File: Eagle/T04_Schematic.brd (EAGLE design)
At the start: 40.6 x 63.5 mm, 29 parts, among them Y1 16 MHz

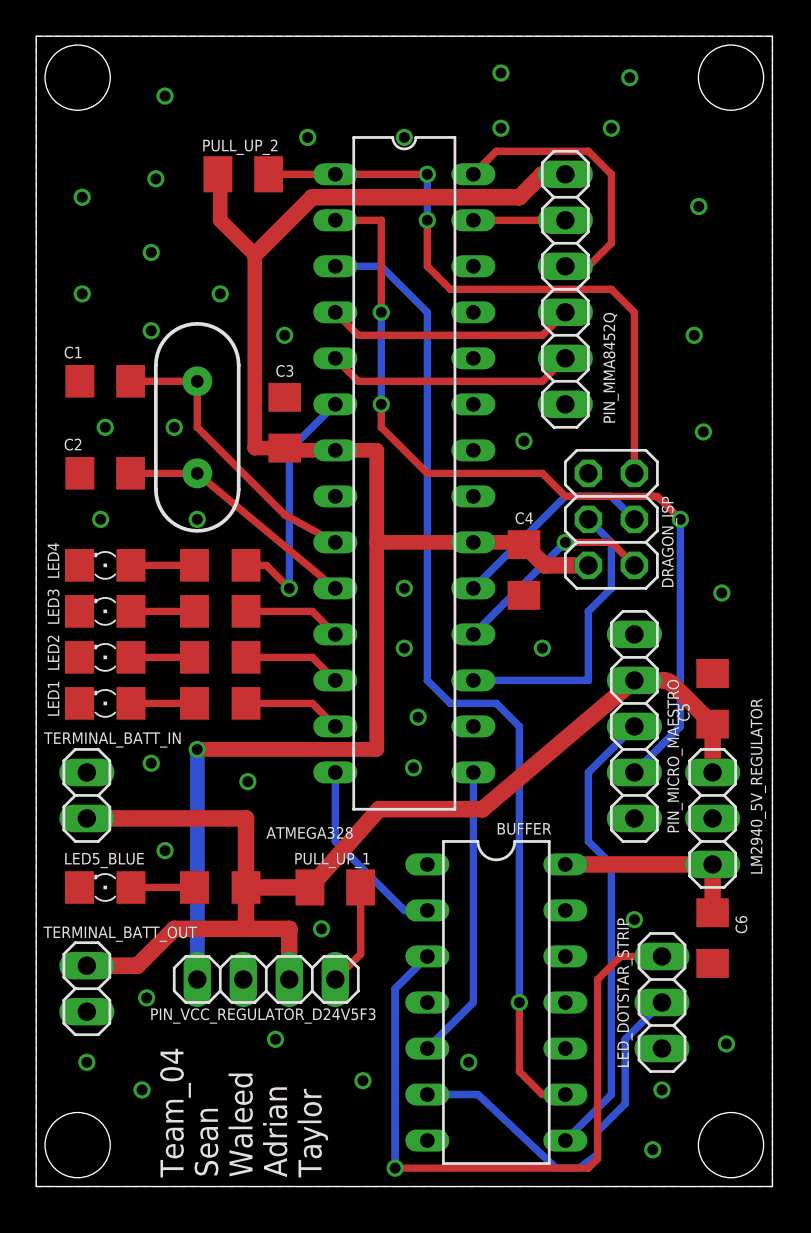
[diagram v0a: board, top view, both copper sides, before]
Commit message: Final(?) Layout
Increase board size for more room to solder.
Improved power signal layout.
Added missing GND and VCC to Dotstar LEDs.
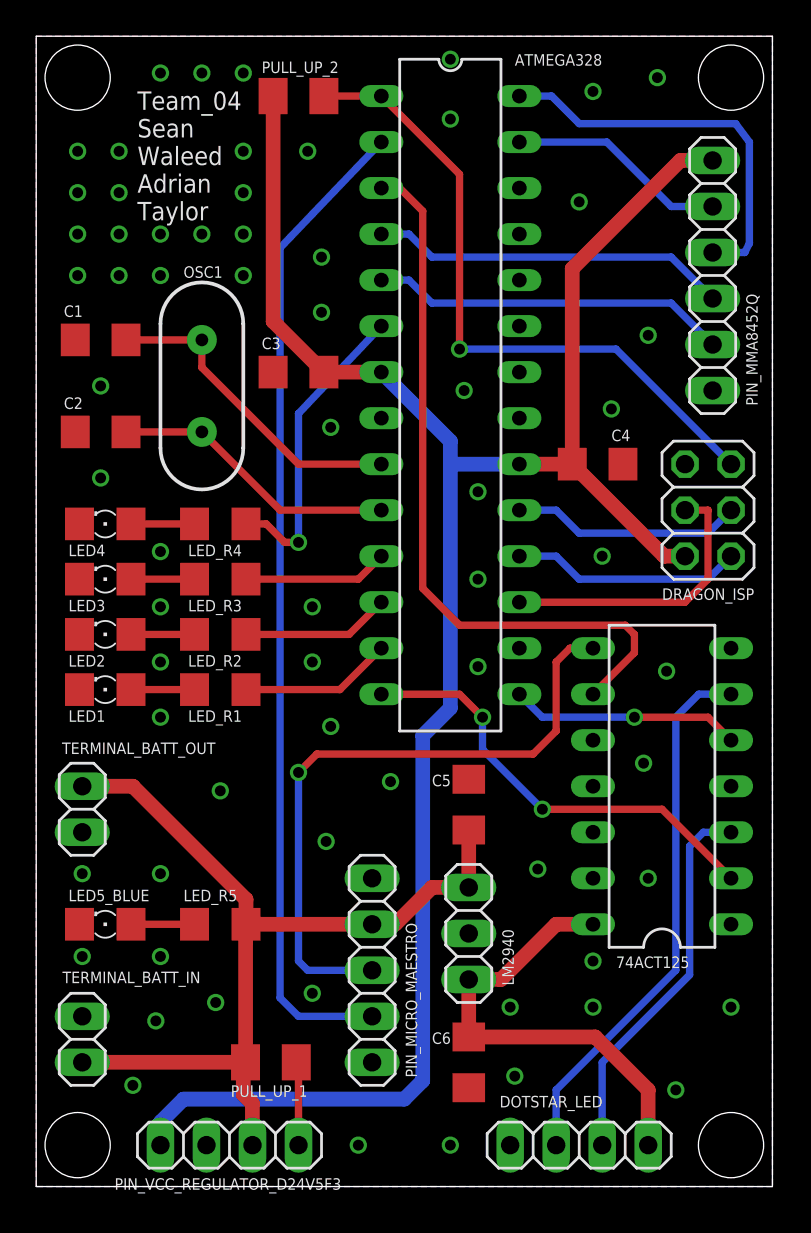
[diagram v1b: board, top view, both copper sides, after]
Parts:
- removed BUFFER: 74ACT125N, 74xx-eu:DIL14
- removed LED_DOTSTAR_STRIP: 1x3, pinhead:1X03
- removed LED_RESISTOR_1, LED_RESISTOR_2, LED_RESISTOR_3, LED_RESISTOR_4, LED_RESISTOR_5: TBD Resistance, rcl:R1206
- removed LM2940_5V_REGULATOR: (no value), pinhead:1X03
- removed Y1: 16 MHz, SparkFun-FreqCtrl:HC49US
- added 74ACT125: 74ACT125N, 74xx-eu:DIL14
- added DOTSTAR_LED: 1x4, pinhead:1X04
- added LED_R1, LED_R2, LED_R3, LED_R4, LED_R5: TBD Resistance, rcl:R1206
- added LM2940: 1x3, pinhead:1X03
- added OSC1: 16 MHz, SparkFun-FreqCtrl:HC49US
- moved PIN_MICRO_MAESTRO 19.8 mm to (18.5, 11.9)
- moved C6 15.1 mm to (23.9, 6.86)
- moved C5 14.7 mm to (23.9, 21.1)
- moved TERMINAL_BATT_IN 13.5 mm to (2.54, 8.13)
- moved PULL_UP_1 10.3 mm to (13.0, 6.86)
- moved TERMINAL_BATT_OUT 9.91 mm to (2.54, 20.8)
- moved PIN_VCC_REGULATOR_D24V5F3 9.37 mm to (10.7, 2.29)
- moved PIN_MMA8452Q 8.16 mm to (37.3, 50.3)
- moved C4 7.12 mm to (31.0, 39.9), turned to 0 degrees
- moved DRAGON_ISP 5.36 mm to (37.1, 37.3)
- moved PULL_UP_2 5.29 mm to (14.5, 60.2)
- moved ATMEGA328 5.01 mm to (22.9, 43.7)
- moved C3 2.90 mm to (14.5, 45.0), turned to 180 degrees
- moved C2 2.30 mm to (3.56, 41.7)
- moved C1 2.30 mm to (3.56, 46.7)
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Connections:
- net 5V_VCC: now also 74ACT125.14, DOTSTAR_LED.1, LM2940.3; no longer BUFFER.14, LM2940_5V_REGULATOR.3
- net CLOCK: now also 74ACT125.2; no longer BUFFER.2
- net DATA: now also 74ACT125.5; no longer BUFFER.5
- net GND: now also 74ACT125.1, 74ACT125.10, 74ACT125.4, 74ACT125.7, DOTSTAR_LED.4, LM2940.2; no longer BUFFER.1, BUFFER.10, BUFFER.4, BUFFER.7, LED_DOTSTAR_STRIP.3, LM2940_5V_REGULATOR.2
- net N$1: now also LED_R5.2; no longer LED_RESISTOR_5.2
- net N$10: now also LED_R2.1; no longer LED_RESISTOR_2.1
- net N$11: now also LED_R4.1; no longer LED_RESISTOR_4.1
- net N$12: now also LED_R1.1; no longer LED_RESISTOR_1.1
- net N$13: now also 74ACT125.6, DOTSTAR_LED.3; no longer BUFFER.6, LED_DOTSTAR_STRIP.2
- net N$2: now also LED_R1.2; no longer LED_RESISTOR_1.2
- net N$3: now also LED_R2.2; no longer LED_RESISTOR_2.2
- net N$4: now also LED_R3.2; no longer LED_RESISTOR_3.2
- net N$5: now also LED_R4.2; no longer LED_RESISTOR_4.2
- net N$8: now also 74ACT125.3, DOTSTAR_LED.2; no longer BUFFER.3, LED_DOTSTAR_STRIP.1
- net N$9: now also LED_R3.1; no longer LED_RESISTOR_3.1
- net RXD: now also 74ACT125.8; no longer BUFFER.8
- net UP_TXD: now also 74ACT125.9; no longer BUFFER.9
- net VCC_6V: now also LED_R5.1, LM2940.1; no longer LED_RESISTOR_5.1, LM2940_5V_REGULATOR.1
- net XTAL1: now also OSC1.1; no longer Y1.1
- net XTAL2: now also OSC1.2; no longer Y1.2
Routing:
- net VCC: track 93.1 -> 113.7 mm, vias 1 -> 0
- net N$8: track 37.8 -> 21.1 mm, vias 1 -> 0
- net 5V_VCC: track 10.8 -> 25.5 mm
- net CLOCK: track 10.5 -> 24.6 mm, vias 0 -> 2
- net UP_TXD: track 54.7 -> 40.6 mm, vias 1 -> 0
- net VCC_6V: track 63.6 -> 50.8 mm
- net RXD: track 25.5 -> 36.0 mm, vias 0 -> 1
- net N$13: track 21.1 -> 29.9 mm
- net SERVO_TXD: track 47.8 -> 55.0 mm, vias 3 -> 0
- net SDA: track 5.08 -> 12.1 mm
- net SCL: track 15.5 -> 21.8 mm
- net INT0: track 13.8 -> 19.8 mm
- net INT1: track 13.8 -> 19.8 mm
- net DATA: track 16.3 -> 12.7 mm, vias 0 -> 1
- net N$12: track 5.45 -> 8.41 mm
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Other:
- board text removed: "Expand to fit space: 1.6'' x 2.5'' Make it easier to solder"

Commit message: Fixed Typo in Component Name
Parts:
- renumbered PIN_VCC_REGULATOR_D24V5F3 to D24V5F3
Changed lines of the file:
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@@
 <attribute name="NAME" x="39.8272" y="43.1038" size="0.635" layer="25" ratio="10" rot="R90"/>
 </element>
-<element name="PIN_VCC_REGULATOR_D24V5F3" library="pinhead" package="1X04" value="1x4" x="10.668" y="2.286" smashed="yes" rot="R180">
-<attribute name="NAME" x="16.8402" y="0.4572" size="0.635" layer="25" ratio="10" rot="R180"/>
+<element name="D24V5F3" library="pinhead" package="1X04" value="1x4" x="10.668" y="2.286" smashed="yes" rot="R180">
+<attribute name="NAME" x="6.2738" y="4.1148" size="0.635" layer="25" ratio="10"/>
 </element>
 <element name="PULL_UP_1" library="rcl" package="M1206" value="10K" x="12.954" y="6.858" smashed="yes" rot="R180">
@@
 <contactref element="LED3" pad="C"/>
 <contactref element="LED4" pad="C"/>
-<contactref element="PIN_VCC_REGULATOR_D24V5F3" pad="3"/>
+<contactref element="D24V5F3" pad="3"/>
 <contactref element="TERMINAL_BATT_OUT" pad="2"/>
 <contactref element="PIN_MICRO_MAESTRO" pad="1"/>
@@
 </signal>
 <signal name="VCC">
-<contactref element="PIN_VCC_REGULATOR_D24V5F3" pad="4"/>
+<contactref element="D24V5F3" pad="4"/>
 <contactref element="PULL_UP_2" pad="2"/>
 <contactref element="ATMEGA328" pad="20"/>
@@
 </signal>
 <signal name="V_REG_RESET">
-<contactref element="PIN_VCC_REGULATOR_D24V5F3" pad="1"/>
+<contactref element="D24V5F3" pad="1"/>
 <contactref element="PULL_UP_1" pad="1"/>
 <wire x1="14.354" y1="6.858" x2="14.478" y2="6.734" width="0.4064" layer="1"/>
@@
 <contactref element="TERMINAL_BATT_IN" pad="2"/>
 <contactref element="TERMINAL_BATT_OUT" pad="1"/>
-<contactref element="PIN_VCC_REGULATOR_D24V5F3" pad="2"/>
+<contactref element="D24V5F3" pad="2"/>
 <contactref element="PULL_UP_1" pad="2"/>
 <contactref element="PIN_MICRO_MAESTRO" pad="2"/>

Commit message: Minor Tweaks and Fixes
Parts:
- moved C4 0.25 mm to (31.2, 39.9)
- renumbered PIN_MICRO_MAESTRO to MICRO_MAESTRO, PIN_MMA8452Q to MMA8452Q
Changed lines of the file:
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@@
 <layer number="17" name="Pads" color="2" fill="1" visible="yes" active="yes"/>
 <layer number="18" name="Vias" color="2" fill="1" visible="yes" active="yes"/>
-<layer number="19" name="Unrouted" color="6" fill="1" visible="yes" active="yes"/>
+<layer number="19" name="Unrouted" color="6" fill="1" visible="no" active="yes"/>
 <layer number="20" name="Dimension" color="15" fill="1" visible="yes" active="yes"/>
 <layer number="21" name="tPlace" color="7" fill="1" visible="yes" active="yes"/>
@@
 <layer number="45" name="Holes" color="7" fill="1" visible="yes" active="yes"/>
 <layer number="46" name="Milling" color="3" fill="1" visible="no" active="yes"/>
-<layer number="47" name="Measures" color="7" fill="1" visible="yes" active="yes"/>
-<layer number="48" name="Document" color="7" fill="1" visible="yes" active="yes"/>
-<layer number="49" name="Reference" color="7" fill="1" visible="yes" active="yes"/>
+<layer number="47" name="Measures" color="7" fill="1" visible="no" active="yes"/>
+<layer number="48" name="Document" color="7" fill="1" visible="no" active="yes"/>
+<layer number="49" name="Reference" color="7" fill="1" visible="no" active="yes"/>
 <layer number="50" name="dxf" color="7" fill="1" visible="no" active="no"/>
 <layer number="51" name="tDocu" color="7" fill="1" visible="yes" active="yes"/>
@@
 Adrian
 Taylor</text>
-<hole x="2.286" y="61.214" drill="3.6"/>
-<hole x="38.354" y="61.214" drill="3.6"/>
-<hole x="2.286" y="2.286" drill="3.6"/>
-<hole x="38.354" y="2.286" drill="3.6"/>
+<hole x="2.286" y="61.214" drill="2.921"/>
+<hole x="38.354" y="61.214" drill="2.921"/>
+<hole x="2.286" y="2.286" drill="2.921"/>
+<hole x="38.354" y="2.286" drill="2.921"/>
 </plain>
 <attributes>
@@
 <attribute name="VALUE" x="34.925" y="12.573" size="0.6096" layer="27" ratio="10" rot="R180"/>
 </element>
-<element name="C4" library="rcl" package="C1206" value="100 nF" x="30.988" y="39.878" smashed="yes">
-<attribute name="NAME" x="31.75" y="41.148" size="0.635" layer="25"/>
-<attribute name="VALUE" x="28.448" y="42.418" size="0.6096" layer="27"/>
+<element name="C4" library="rcl" package="C1206" value="100 nF" x="31.242" y="39.878" smashed="yes">
+<attribute name="NAME" x="32.004" y="41.148" size="0.635" layer="25"/>
+<attribute name="VALUE" x="28.702" y="42.418" size="0.6096" layer="27"/>
 </element>
 <element name="C3" library="rcl" package="C1206" value="100 nF" x="14.478" y="44.958" smashed="yes" rot="R180">
@@
 <attribute name="VALUE" x="11.43" y="17.018" size="1.27" layer="27" rot="R180"/>
 </element>
-<element name="PIN_MICRO_MAESTRO" library="pinhead" package="1X05" value="1x5" x="18.542" y="11.938" smashed="yes" rot="R270">
+<element name="MICRO_MAESTRO" library="pinhead" package="1X05" value="1x5" x="18.542" y="11.938" smashed="yes" rot="R270">
 <attribute name="NAME" x="21.0312" y="6.0198" size="0.635" layer="25" ratio="10" rot="R90"/>
 </element>
-<element name="PIN_MMA8452Q" library="pinhead" package="1X06" value="1x6" x="37.338" y="50.292" smashed="yes" rot="R270">
+<element name="MMA8452Q" library="pinhead" package="1X06" value="1x6" x="37.338" y="50.292" smashed="yes" rot="R270">
 <attribute name="NAME" x="39.8272" y="43.1038" size="0.635" layer="25" ratio="10" rot="R90"/>
 </element>
@@
 <contactref element="ATMEGA328" pad="8"/>
 <contactref element="TERMINAL_BATT_IN" pad="1"/>
-<contactref element="PIN_MMA8452Q" pad="6"/>
+<contactref element="MMA8452Q" pad="6"/>
 <contactref element="C4" pad="2"/>
 <contactref element="C3" pad="2"/>
@@
 <contactref element="D24V5F3" pad="3"/>
 <contactref element="TERMINAL_BATT_OUT" pad="2"/>
-<contactref element="PIN_MICRO_MAESTRO" pad="1"/>
+<contactref element="MICRO_MAESTRO" pad="1"/>
 <contactref element="LED5_BLUE" pad="C"/>
 <contactref element="C1" pad="2"/>
@@
 <contactref element="C3" pad="1"/>
 <contactref element="ATMEGA328" pad="7"/>
-<contactref element="PIN_MMA8452Q" pad="1"/>
+<contactref element="MMA8452Q" pad="1"/>
 <contactref element="DRAGON_ISP" pad="2"/>
 <wire x1="21.336" y1="24.892" x2="22.86" y2="26.416" width="0.8128" layer="16"/>
@@
 <wire x1="15.878" y1="44.958" x2="13.078" y2="47.758" width="0.8128" layer="1"/>
 <wire x1="13.078" y1="47.758" x2="13.078" y2="60.198" width="0.8128" layer="1"/>
-<wire x1="26.67" y1="39.878" x2="29.588" y2="39.878" width="0.8128" layer="1"/>
-<wire x1="29.588" y1="39.878" x2="34.668" y2="34.798" width="0.8128" layer="1"/>
+<wire x1="26.67" y1="39.878" x2="29.842" y2="39.878" width="0.8128" layer="1"/>
+<wire x1="29.842" y1="39.878" x2="34.668" y2="34.798" width="0.8128" layer="1"/>
 <wire x1="34.668" y1="34.798" x2="35.814" y2="34.798" width="0.8128" layer="1"/>
-<wire x1="29.588" y1="39.878" x2="29.588" y2="50.67" width="0.8128" layer="1"/>
-<wire x1="29.588" y1="50.67" x2="35.56" y2="56.642" width="0.8128" layer="1"/>
+<wire x1="29.842" y1="39.878" x2="29.842" y2="50.67" width="0.8128" layer="1"/>
+<wire x1="29.842" y1="50.67" x2="35.56" y2="56.642" width="0.8128" layer="1"/>
 <wire x1="35.56" y1="56.642" x2="37.338" y2="56.642" width="0.8128" layer="1"/>
 <wire x1="21.336" y1="5.842" x2="21.336" y2="24.892" width="0.8128" layer="16"/>
@@
 </signal>
 <signal name="SDA">
-<contactref element="PIN_MMA8452Q" pad="2"/>
+<contactref element="MMA8452Q" pad="2"/>
 <contactref element="ATMEGA328" pad="27"/>
 <wire x1="26.67" y1="57.658" x2="31.496" y2="57.658" width="0.4064" layer="16"/>
@@
 </signal>
 <signal name="SCL">
-<contactref element="PIN_MMA8452Q" pad="3"/>
+<contactref element="MMA8452Q" pad="3"/>
 <contactref element="ATMEGA328" pad="28"/>
 <wire x1="37.338" y1="51.562" x2="39.116" y2="51.562" width="0.4064" layer="16"/>
@@
 </signal>
 <signal name="INT0">
-<contactref element="PIN_MMA8452Q" pad="4"/>
+<contactref element="MMA8452Q" pad="4"/>
 <contactref element="ATMEGA328" pad="4"/>
 <wire x1="37.338" y1="49.022" x2="35.052" y2="51.308" width="0.4064" layer="16"/>
@@
 <signal name="INT1">
 <contactref element="ATMEGA328" pad="5"/>
-<contactref element="PIN_MMA8452Q" pad="5"/>
+<contactref element="MMA8452Q" pad="5"/>
 <wire x1="37.338" y1="46.482" x2="35.052" y2="48.768" width="0.4064" layer="16"/>
 <wire x1="35.052" y1="48.768" x2="21.844" y2="48.768" width="0.4064" layer="16"/>
@@
 </signal>
 <signal name="RXD">
-<contactref element="PIN_MICRO_MAESTRO" pad="3"/>
+<contactref element="MICRO_MAESTRO" pad="3"/>
 <contactref element="74ACT125" pad="8"/>
 <wire x1="18.542" y1="11.938" x2="14.986" y2="11.938" width="0.4064" layer="16"/>
@@
 </signal>
 <signal name="SERVO_TXD">
-<contactref element="PIN_MICRO_MAESTRO" pad="4"/>
+<contactref element="MICRO_MAESTRO" pad="4"/>
 <contactref element="ATMEGA328" pad="2"/>
 <wire x1="19.05" y1="57.658" x2="13.462" y2="51.816" width="0.4064" layer="16"/>
@@
 <contactref element="D24V5F3" pad="2"/>
 <contactref element="PULL_UP_1" pad="2"/>
-<contactref element="PIN_MICRO_MAESTRO" pad="2"/>
+<contactref element="MICRO_MAESTRO" pad="2"/>
 <contactref element="LED_R5" pad="1"/>
 <contactref element="C5" pad="1"/>
